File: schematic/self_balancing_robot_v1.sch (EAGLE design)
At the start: 17 parts, among them J1 6_PIN_SERIAL_CABLEPTH, U1 328P, U2 GY-521MPU6050

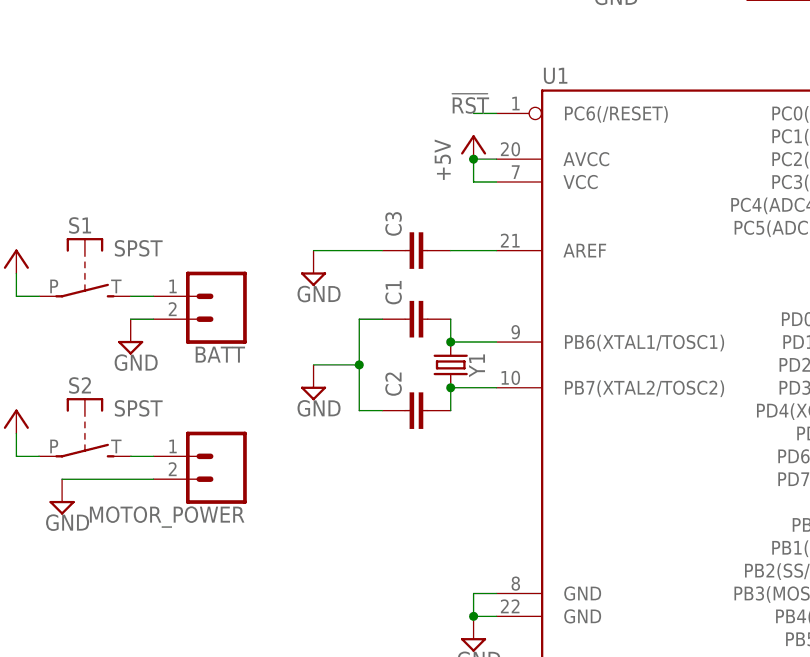
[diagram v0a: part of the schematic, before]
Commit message: Updated with part values
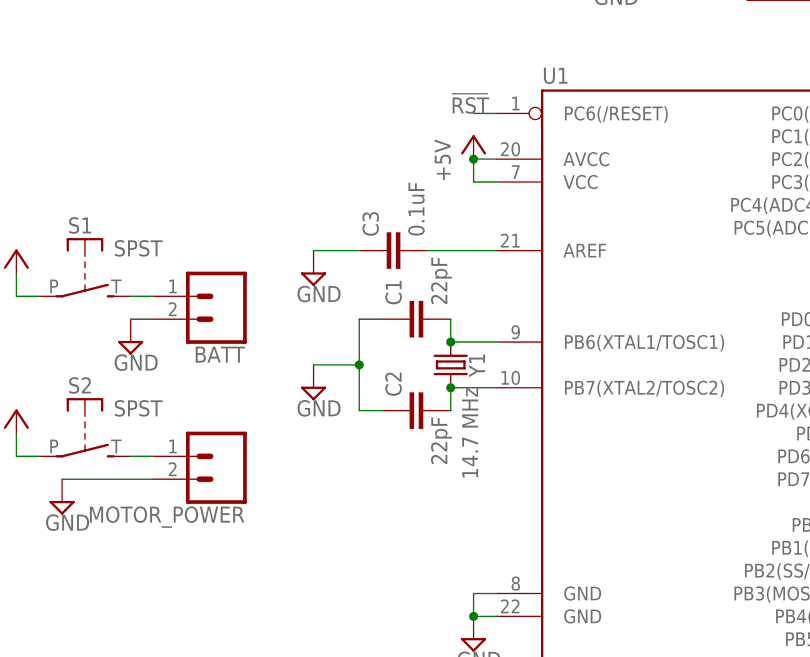
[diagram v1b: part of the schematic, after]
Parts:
- C1, C2: value (none) -> 22pF
- C3: value (none) -> 0.1uF
- Y1: value (none) -> 14.7 MHz
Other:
- moved on the sheet: C3
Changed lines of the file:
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@@
 <parts>
 <part name="U1" library="SparkFun-IC-Microcontroller" library_urn="urn:adsk.eagle:library:525" deviceset="ATMEGA328P_PDIP" device="" package3d_urn="urn:adsk.eagle:package:38942/1" value="328P"/>
-<part name="Y1" library="SparkFun-Clocks" library_urn="urn:adsk.eagle:library:511" deviceset="CRYSTAL" device="PTH-HC49UV" package3d_urn="urn:adsk.eagle:package:37511/1"/>
-<part name="C1" library="resistor" library_urn="urn:adsk.eagle:library:348" deviceset="C-EU" device="025-025X050" package3d_urn="urn:adsk.eagle:package:26151/1"/>
-<part name="C2" library="resistor" library_urn="urn:adsk.eagle:library:348" deviceset="C-EU" device="025-025X050" package3d_urn="urn:adsk.eagle:package:26151/1"/>
-<part name="C3" library="resistor" library_urn="urn:adsk.eagle:library:348" deviceset="C-EU" device="025-025X050" package3d_urn="urn:adsk.eagle:package:26151/1"/>
+<part name="Y1" library="SparkFun-Clocks" library_urn="urn:adsk.eagle:library:511" deviceset="CRYSTAL" device="PTH-HC49UV" package3d_urn="urn:adsk.eagle:package:37511/1" value="14.7 MHz"/>
+<part name="C1" library="resistor" library_urn="urn:adsk.eagle:library:348" deviceset="C-EU" device="025-025X050" package3d_urn="urn:adsk.eagle:package:26151/1" value="22pF"/>
+<part name="C2" library="resistor" library_urn="urn:adsk.eagle:library:348" deviceset="C-EU" device="025-025X050" package3d_urn="urn:adsk.eagle:package:26151/1" value="22pF"/>
+<part name="C3" library="resistor" library_urn="urn:adsk.eagle:library:348" deviceset="C-EU" device="025-025X050" package3d_urn="urn:adsk.eagle:package:26151/1" value="0.1uF"/>
 <part name="ISP" library="adafruit" library_urn="urn:adsk.eagle:library:420" deviceset="AVRISP" device="-BOX"/>
 <part name="J1" library="SparkFun-Connectors" library_urn="urn:adsk.eagle:library:513" deviceset="6_PIN_SERIAL_CABLE" device="PTH" package3d_urn="urn:adsk.eagle:package:38027/1"/>
@@
 <instances>
 <instance part="U1" gate="G$1" x="45.72" y="35.56"/>
-<instance part="Y1" gate="G$1" x="17.78" y="33.02" rot="R270"/>
+<instance part="Y1" gate="G$1" x="17.78" y="33.02" smashed="yes" rot="R270">
+<attribute name="NAME" x="19.812" y="33.02" size="1.778" layer="95" font="vector" rot="R270" align="bottom-center"/>
+<attribute name="VALUE" x="20.828" y="25.4" size="1.778" layer="96" font="vector" rot="R270" align="top-center"/>
+</instance>
 <instance part="C1" gate="G$1" x="12.7" y="38.1" rot="R90"/>
-<instance part="C2" gate="G$1" x="12.7" y="27.94" rot="R90"/>
-<instance part="C3" gate="G$1" x="12.7" y="45.72" rot="R90"/>
+<instance part="C2" gate="G$1" x="12.7" y="27.94" smashed="yes" rot="R90">
+<attribute name="NAME" x="12.319" y="29.464" size="1.778" layer="95" rot="R90"/>
+<attribute name="VALUE" x="17.399" y="21.844" size="1.778" layer="96" rot="R90"/>
+</instance>
+<instance part="C3" gate="G$1" x="10.16" y="45.72" rot="R90"/>
 <instance part="ISP" gate="G$1" x="17.78" y="83.82"/>
 <instance part="J1" gate="G$1" x="60.96" y="78.74" rot="R90"/>
@@
 <pinref part="C3" gate="G$1" pin="1"/>
 <pinref part="SUPPLY3" gate="GND" pin="GND"/>
-<wire x1="10.16" y1="45.72" x2="2.54" y2="45.72" width="0.1524" layer="91"/>
+<wire x1="7.62" y1="45.72" x2="2.54" y2="45.72" width="0.1524" layer="91"/>
 </segment>
 <segment>
@@
 <pinref part="C3" gate="G$1" pin="2"/>
 <pinref part="U1" gate="G$1" pin="AREF"/>
-<wire x1="17.78" y1="45.72" x2="22.86" y2="45.72" width="0.1524" layer="91"/>
+<wire x1="15.24" y1="45.72" x2="22.86" y2="45.72" width="0.1524" layer="91"/>
 </segment>
 </net>

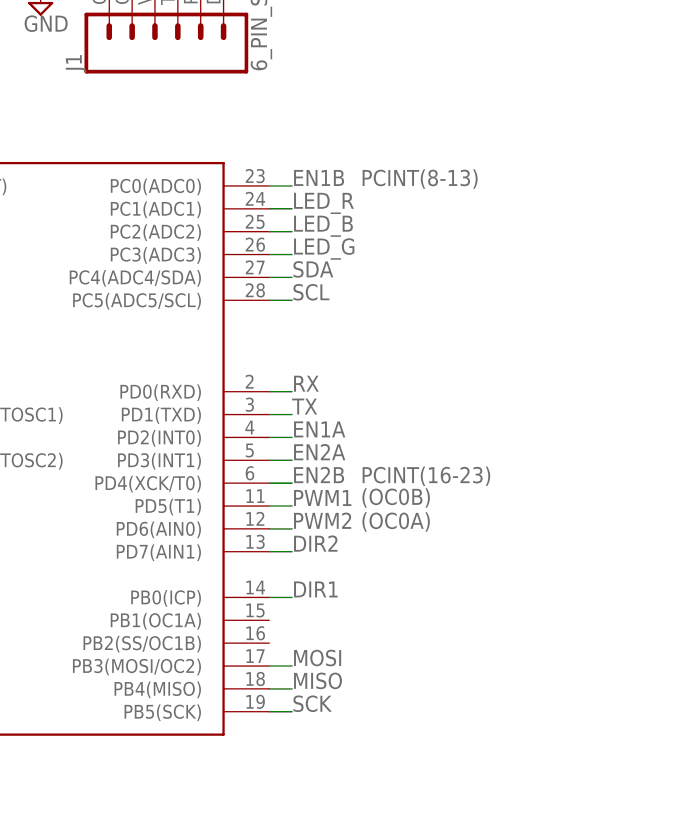
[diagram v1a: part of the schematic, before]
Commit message: updated schematic for ENC change
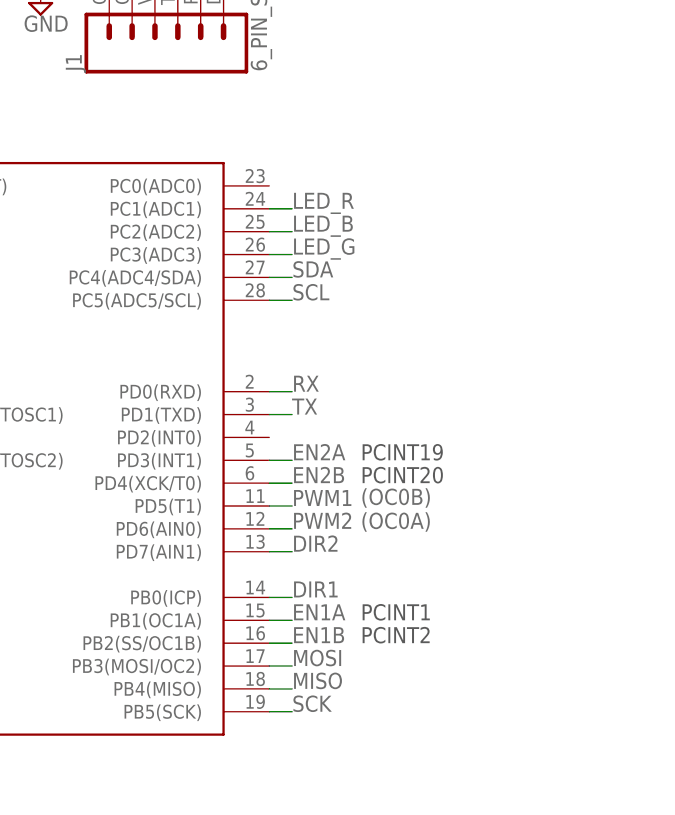
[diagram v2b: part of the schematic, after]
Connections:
- net EN1A: now also U1.PB1(OC1A); no longer U1.PD2(INT0)
- net EN1B: now also U1.PB2(SS/OC1B); no longer U1.PC0(ADC0)
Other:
- note added: "PCINT1"
- note added: "PCINT19"
- note added: "PCINT2"
- note added: "PCINT20"
- note removed: "PCINT(16-23)"
- note removed: "PCINT(8-13)"
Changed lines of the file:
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@@
 <text x="81.28" y="22.86" size="1.778" layer="96">(OC0B)
 (OC0A)</text>
-<text x="81.28" y="60.96" size="1.778" layer="95">PCINT(8-13)</text>
-<text x="81.28" y="27.94" size="1.778" layer="95">PCINT(16-23)</text>
 <text x="12.7" y="114.3" size="2.54" layer="95">Self Balancing Robot v1.0</text>
 <frame x1="-50.8" y1="-73.66" x2="111.76" y2="127" columns="8" rows="5" layer="97"/>
+<text x="81.28" y="30.48" size="1.778" layer="97">PCINT19</text>
+<text x="81.28" y="27.94" size="1.778" layer="97">PCINT20</text>
+<text x="81.28" y="12.7" size="1.778" layer="97">PCINT1</text>
+<text x="81.28" y="10.16" size="1.778" layer="97">PCINT2</text>
 </plain>
 <instances>
@@
 </segment>
 <segment>
-<pinref part="U1" gate="G$1" pin="PD2(INT0)"/>
-<wire x1="71.12" y1="33.02" x2="73.66" y2="33.02" width="0.1524" layer="91"/>
-<label x="73.66" y="33.02" size="1.778" layer="95"/>
+<pinref part="U1" gate="G$1" pin="PB1(OC1A)"/>
+<wire x1="71.12" y1="12.7" x2="73.66" y2="12.7" width="0.1524" layer="91"/>
+<label x="73.66" y="12.7" size="1.778" layer="95"/>
 </segment>
 </net>
@@
 </segment>
 <segment>
-<pinref part="U1" gate="G$1" pin="PC0(ADC0)"/>
-<wire x1="71.12" y1="60.96" x2="73.66" y2="60.96" width="0.1524" layer="91"/>
-<label x="73.66" y="60.96" size="1.778" layer="95"/>
-</segment>
-</net>
+<pinref part="U1" gate="G$1" pin="PB2(SS/OC1B)"/>
+<wire x1="71.12" y1="10.16" x2="73.66" y2="10.16" width="0.1524" layer="91"/>
+<label x="73.66" y="10.16" size="1.778" layer="95"/>
+</segment>
+</net>

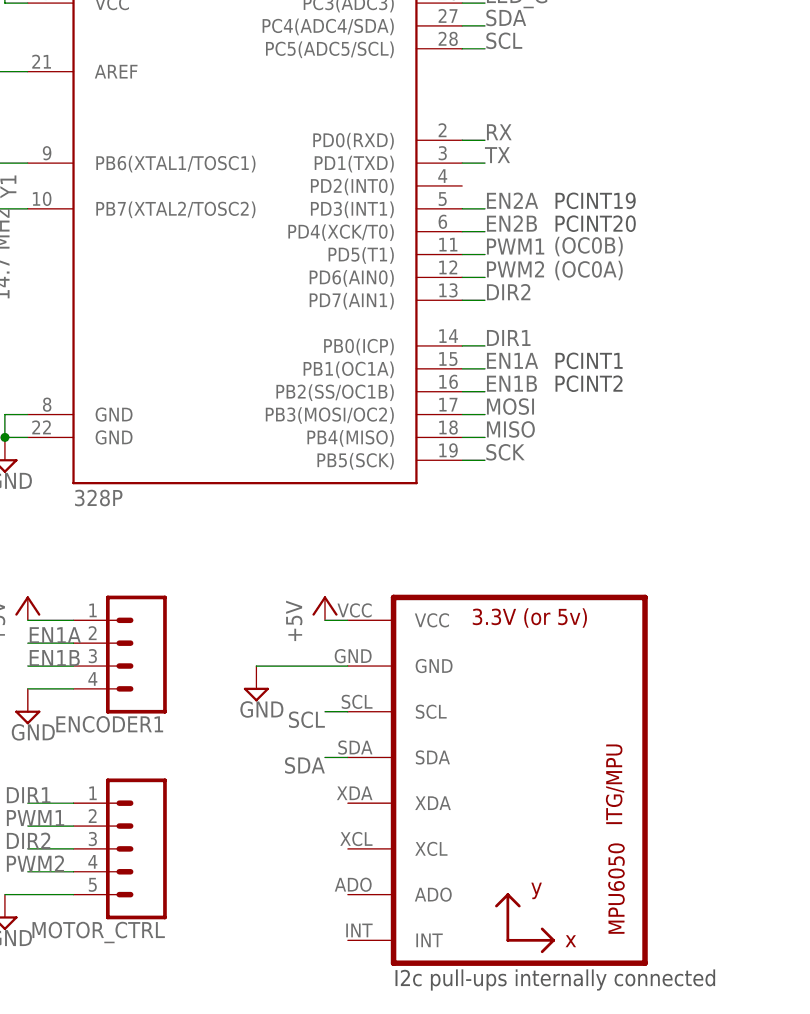
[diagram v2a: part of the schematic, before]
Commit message: updated schematic with INT pin for IMU
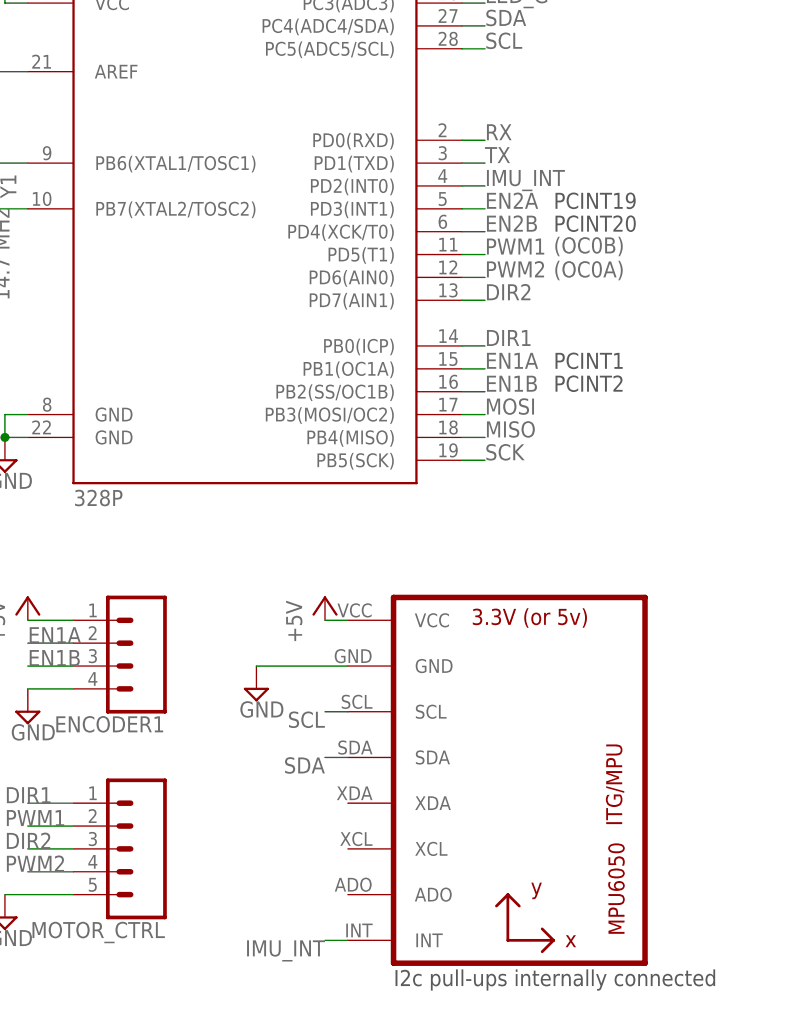
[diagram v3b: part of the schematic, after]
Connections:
- new net IMU_INT: U1.PD2(INT0), U2.INT
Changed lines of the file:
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@@
+</segment>
+</net>
+<net name="IMU_INT" class="0">
+<segment>
+<pinref part="U2" gate="G$1" pin="INT"/>
+<wire x1="58.42" y1="-50.8" x2="55.88" y2="-50.8" width="0.1524" layer="91"/>
+<label x="55.88" y="-50.8" size="1.778" layer="95" rot="R180"/>
+</segment>
+<segment>
+<pinref part="U1" gate="G$1" pin="PD2(INT0)"/>
+<wire x1="71.12" y1="33.02" x2="73.66" y2="33.02" width="0.1524" layer="91"/>
+<label x="73.66" y="33.02" size="1.778" layer="95"/>
 </segment>
 </net>
